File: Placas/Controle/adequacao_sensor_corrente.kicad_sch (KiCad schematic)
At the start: 10 parts, among them J8 Conn_01x03_Pin, U6 LM324

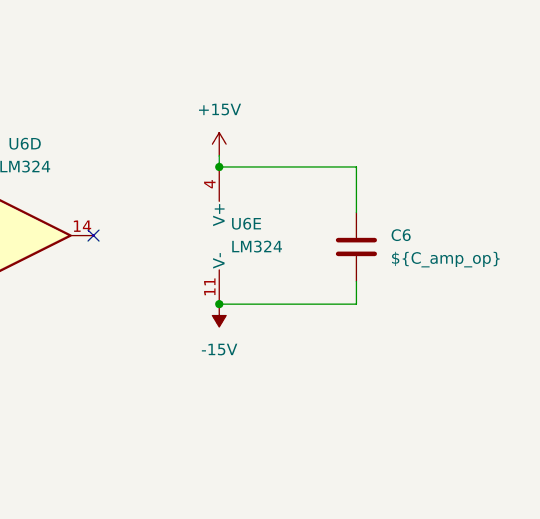
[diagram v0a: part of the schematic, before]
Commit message: Adição de circuitos opcionais para PWM
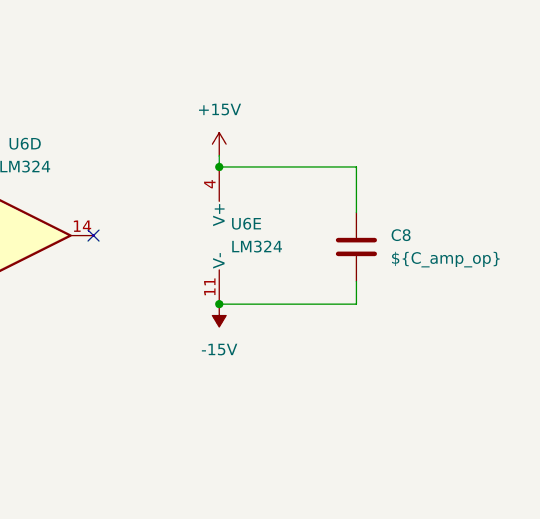
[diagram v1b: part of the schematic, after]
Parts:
- renumbered C6 to C8
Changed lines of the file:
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@@
 		(dnp no)
 		(fields_autoplaced yes)
-		(property "Reference" "#PWR38"
+		(property "Reference" "#PWR40"
 			(at 53.34 63.5 0)
 			(effects
@@
 			(project "board"
 				(path "/01568b53-f202-4f02-9c1a-9c10c7610b4b/64ed1ee1-6201-4cd1-840c-b46b599d55ab/0ec4e805-f770-43f6-9ceb-79230d0ce8bc"
-					(reference "#PWR38")
+					(reference "#PWR40")
 					(unit 1)
 				)
 				(path "/01568b53-f202-4f02-9c1a-9c10c7610b4b/64ed1ee1-6201-4cd1-840c-b46b599d55ab/23b832df-fa68-4730-aab0-9fb63a0aaa4a"
-					(reference "#PWR46")
+					(reference "#PWR48")
 					(unit 1)
 				)
 				(path "/01568b53-f202-4f02-9c1a-9c10c7610b4b/64ed1ee1-6201-4cd1-840c-b46b599d55ab/54eee298-1ebc-4f78-aeba-50023d2029d6"
-					(reference "#PWR22")
+					(reference "#PWR24")
 					(unit 1)
 				)
 				(path "/01568b53-f202-4f02-9c1a-9c10c7610b4b/64ed1ee1-6201-4cd1-840c-b46b599d55ab/6bc42b43-1f09-4868-86cc-13b6bc39566b"
-					(reference "#PWR30")
+					(reference "#PWR32")
 					(unit 1)
 				)
@@
 		(dnp no)
 		(fields_autoplaced yes)
-		(property "Reference" "#PWR43"
+		(property "Reference" "#PWR45"
 			(at 207.01 85.09 0)
 			(effects
@@
 			(project "board"
 				(path "/01568b53-f202-4f02-9c1a-9c10c7610b4b/64ed1ee1-6201-4cd1-840c-b46b599d55ab/0ec4e805-f770-43f6-9ceb-79230d0ce8bc"
-					(reference "#PWR43")
+					(reference "#PWR45")
 					(unit 1)
 				)
 				(path "/01568b53-f202-4f02-9c1a-9c10c7610b4b/64ed1ee1-6201-4cd1-840c-b46b599d55ab/23b832df-fa68-4730-aab0-9fb63a0aaa4a"
-					(reference "#PWR51")
+					(reference "#PWR53")
 					(unit 1)
 				)
 				(path "/01568b53-f202-4f02-9c1a-9c10c7610b4b/64ed1ee1-6201-4cd1-840c-b46b599d55ab/54eee298-1ebc-4f78-aeba-50023d2029d6"
-					(reference "#PWR27")
+					(reference "#PWR29")
 					(unit 1)
 				)
 				(path "/01568b53-f202-4f02-9c1a-9c10c7610b4b/64ed1ee1-6201-4cd1-840c-b46b599d55ab/6bc42b43-1f09-4868-86cc-13b6bc39566b"
-					(reference "#PWR35")
+					(reference "#PWR37")
 					(unit 1)
 				)
@@
 		(dnp no)
 		(fields_autoplaced yes)
-		(property "Reference" "C6"
+		(property "Reference" "C8"
 			(at 226.06 81.2799 0)
 			(effects
@@
 			(project "board"
 				(path "/01568b53-f202-4f02-9c1a-9c10c7610b4b/64ed1ee1-6201-4cd1-840c-b46b599d55ab/0ec4e805-f770-43f6-9ceb-79230d0ce8bc"
+					(reference "C8")
+					(unit 1)
+				)
+				(path "/01568b53-f202-4f02-9c1a-9c10c7610b4b/64ed1ee1-6201-4cd1-840c-b46b599d55ab/23b832df-fa68-4730-aab0-9fb63a0aaa4a"
+					(reference "C9")
+					(unit 1)
+				)
+				(path "/01568b53-f202-4f02-9c1a-9c10c7610b4b/64ed1ee1-6201-4cd1-840c-b46b599d55ab/54eee298-1ebc-4f78-aeba-50023d2029d6"
 					(reference "C6")
 					(unit 1)
 				)
-				(path "/01568b53-f202-4f02-9c1a-9c10c7610b4b/64ed1ee1-6201-4cd1-840c-b46b599d55ab/23b832df-fa68-4730-aab0-9fb63a0aaa4a"
+				(path "/01568b53-f202-4f02-9c1a-9c10c7610b4b/64ed1ee1-6201-4cd1-840c-b46b599d55ab/6bc42b43-1f09-4868-86cc-13b6bc39566b"
 					(reference "C7")
-					(unit 1)
-				)
-				(path "/01568b53-f202-4f02-9c1a-9c10c7610b4b/64ed1ee1-6201-4cd1-840c-b46b599d55ab/54eee298-1ebc-4f78-aeba-50023d2029d6"
-					(reference "C4")
-					(unit 1)
-				)
-				(path "/01568b53-f202-4f02-9c1a-9c10c7610b4b/64ed1ee1-6201-4cd1-840c-b46b599d55ab/6bc42b43-1f09-4868-86cc-13b6bc39566b"
-					(reference "C5")
 					(unit 1)
 				)
@@
 		(dnp no)
 		(fields_autoplaced yes)
-		(property "Reference" "#PWR36"
+		(property "Reference" "#PWR38"
 			(at 52.07 83.82 0)
 			(effects
@@
 			(project "board"
 				(path "/01568b53-f202-4f02-9c1a-9c10c7610b4b/64ed1ee1-6201-4cd1-840c-b46b599d55ab/0ec4e805-f770-43f6-9ceb-79230d0ce8bc"
-					(reference "#PWR36")
+					(reference "#PWR38")
 					(unit 1)
 				)
 				(path "/01568b53-f202-4f02-9c1a-9c10c7610b4b/64ed1ee1-6201-4cd1-840c-b46b599d55ab/23b832df-fa68-4730-aab0-9fb63a0aaa4a"
-					(reference "#PWR44")
+					(reference "#PWR46")
 					(unit 1)
 				)
 				(path "/01568b53-f202-4f02-9c1a-9c10c7610b4b/64ed1ee1-6201-4cd1-840c-b46b599d55ab/54eee298-1ebc-4f78-aeba-50023d2029d6"
-					(reference "#PWR20")
+					(reference "#PWR22")
 					(unit 1)
 				)
 				(path "/01568b53-f202-4f02-9c1a-9c10c7610b4b/64ed1ee1-6201-4cd1-840c-b46b599d55ab/6bc42b43-1f09-4868-86cc-13b6bc39566b"
-					(reference "#PWR28")
+					(reference "#PWR30")
 					(unit 1)
 				)
@@
 		(dnp no)
 		(fields_autoplaced yes)
-		(property "Reference" "#PWR41"
+		(property "Reference" "#PWR43"
 			(at 121.92 104.14 0)
 			(effects
@@
 			(project "board"
 				(path "/01568b53-f202-4f02-9c1a-9c10c7610b4b/64ed1ee1-6201-4cd1-840c-b46b599d55ab/0ec4e805-f770-43f6-9ceb-79230d0ce8bc"
-					(reference "#PWR41")
+					(reference "#PWR43")
 					(unit 1)
 				)
 				(path "/01568b53-f202-4f02-9c1a-9c10c7610b4b/64ed1ee1-6201-4cd1-840c-b46b599d55ab/23b832df-fa68-4730-aab0-9fb63a0aaa4a"
-					(reference "#PWR49")
+					(reference "#PWR51")
 					(unit 1)
 				)
 				(path "/01568b53-f202-4f02-9c1a-9c10c7610b4b/64ed1ee1-6201-4cd1-840c-b46b599d55ab/54eee298-1ebc-4f78-aeba-50023d2029d6"
-					(reference "#PWR25")
+					(reference "#PWR27")
 					(unit 1)
 				)
 				(path "/01568b53-f202-4f02-9c1a-9c10c7610b4b/64ed1ee1-6201-4cd1-840c-b46b599d55ab/6bc42b43-1f09-4868-86cc-13b6bc39566b"
-					(reference "#PWR33")
+					(reference "#PWR35")
 					(unit 1)
 				)
@@
 		(dnp no)
 		(fields_autoplaced yes)
-		(property "Reference" "#PWR40"
+		(property "Reference" "#PWR42"
 			(at 67.31 85.09 0)
 			(effects
@@
 			(project "board"
 				(path "/01568b53-f202-4f02-9c1a-9c10c7610b4b/64ed1ee1-6201-4cd1-840c-b46b599d55ab/0ec4e805-f770-43f6-9ceb-79230d0ce8bc"
-					(reference "#PWR40")
+					(reference "#PWR42")
 					(unit 1)
 				)
 				(path "/01568b53-f202-4f02-9c1a-9c10c7610b4b/64ed1ee1-6201-4cd1-840c-b46b599d55ab/23b832df-fa68-4730-aab0-9fb63a0aaa4a"
-					(reference "#PWR48")
+					(reference "#PWR50")
 					(unit 1)
 				)
 				(path "/01568b53-f202-4f02-9c1a-9c10c7610b4b/64ed1ee1-6201-4cd1-840c-b46b599d55ab/54eee298-1ebc-4f78-aeba-50023d2029d6"
-					(reference "#PWR24")
+					(reference "#PWR26")
 					(unit 1)
 				)
 				(path "/01568b53-f202-4f02-9c1a-9c10c7610b4b/64ed1ee1-6201-4cd1-840c-b46b599d55ab/6bc42b43-1f09-4868-86cc-13b6bc39566b"
-					(reference "#PWR32")
+					(reference "#PWR34")
 					(unit 1)
 				)
@@
 		(dnp no)
 		(fields_autoplaced yes)
-		(property "Reference" "#PWR39"
+		(property "Reference" "#PWR41"
 			(at 53.34 68.58 0)
 			(effects
@@
 			(project "board"
 				(path "/01568b53-f202-4f02-9c1a-9c10c7610b4b/64ed1ee1-6201-4cd1-840c-b46b599d55ab/0ec4e805-f770-43f6-9ceb-79230d0ce8bc"
-					(reference "#PWR39")
+					(reference "#PWR41")
 					(unit 1)
 				)
 				(path "/01568b53-f202-4f02-9c1a-9c10c7610b4b/64ed1ee1-6201-4cd1-840c-b46b599d55ab/23b832df-fa68-4730-aab0-9fb63a0aaa4a"
-					(reference "#PWR47")
+					(reference "#PWR49")
 					(unit 1)
 				)
 				(path "/01568b53-f202-4f02-9c1a-9c10c7610b4b/64ed1ee1-6201-4cd1-840c-b46b599d55ab/54eee298-1ebc-4f78-aeba-50023d2029d6"
-					(reference "#PWR23")
+					(reference "#PWR25")
 					(unit 1)
 				)
 				(path "/01568b53-f202-4f02-9c1a-9c10c7610b4b/64ed1ee1-6201-4cd1-840c-b46b599d55ab/6bc42b43-1f09-4868-86cc-13b6bc39566b"
-					(reference "#PWR31")
+					(reference "#PWR33")
 					(unit 1)
 				)
@@
 		(dnp no)
 		(fields_autoplaced yes)
-		(property "Reference" "#PWR37"
+		(property "Reference" "#PWR39"
 			(at 52.07 115.57 0)
 			(effects
@@
 			(project "board"
 				(path "/01568b53-f202-4f02-9c1a-9c10c7610b4b/64ed1ee1-6201-4cd1-840c-b46b599d55ab/0ec4e805-f770-43f6-9ceb-79230d0ce8bc"
-					(reference "#PWR37")
+					(reference "#PWR39")
 					(unit 1)
 				)
 				(path "/01568b53-f202-4f02-9c1a-9c10c7610b4b/64ed1ee1-6201-4cd1-840c-b46b599d55ab/23b832df-fa68-4730-aab0-9fb63a0aaa4a"
-					(reference "#PWR45")
+					(reference "#PWR47")
 					(unit 1)
 				)
 				(path "/01568b53-f202-4f02-9c1a-9c10c7610b4b/64ed1ee1-6201-4cd1-840c-b46b599d55ab/54eee298-1ebc-4f78-aeba-50023d2029d6"
-					(reference "#PWR21")
+					(reference "#PWR23")
 					(unit 1)
 				)
 				(path "/01568b53-f202-4f02-9c1a-9c10c7610b4b/64ed1ee1-6201-4cd1-840c-b46b599d55ab/6bc42b43-1f09-4868-86cc-13b6bc39566b"
-					(reference "#PWR29")
+					(reference "#PWR31")
 					(unit 1)
 				)
@@
 		(dnp no)
 		(fields_autoplaced yes)
-		(property "Reference" "#PWR42"
+		(property "Reference" "#PWR44"
 			(at 207.01 76.2 0)
 			(effects
@@
 			(project "board"
 				(path "/01568b53-f202-4f02-9c1a-9c10c7610b4b/64ed1ee1-6201-4cd1-840c-b46b599d55ab/0ec4e805-f770-43f6-9ceb-79230d0ce8bc"
-					(reference "#PWR42")
+					(reference "#PWR44")
 					(unit 1)
 				)
 				(path "/01568b53-f202-4f02-9c1a-9c10c7610b4b/64ed1ee1-6201-4cd1-840c-b46b599d55ab/23b832df-fa68-4730-aab0-9fb63a0aaa4a"
-					(reference "#PWR50")
+					(reference "#PWR52")
 					(unit 1)
 				)
 				(path "/01568b53-f202-4f02-9c1a-9c10c7610b4b/64ed1ee1-6201-4cd1-840c-b46b599d55ab/54eee298-1ebc-4f78-aeba-50023d2029d6"
-					(reference "#PWR26")
+					(reference "#PWR28")
 					(unit 1)
 				)
 				(path "/01568b53-f202-4f02-9c1a-9c10c7610b4b/64ed1ee1-6201-4cd1-840c-b46b599d55ab/6bc42b43-1f09-4868-86cc-13b6bc39566b"
-					(reference "#PWR34")
-					(unit 1)
-				)
+					(reference "#PWR36")
+					(unit 1)
+				)

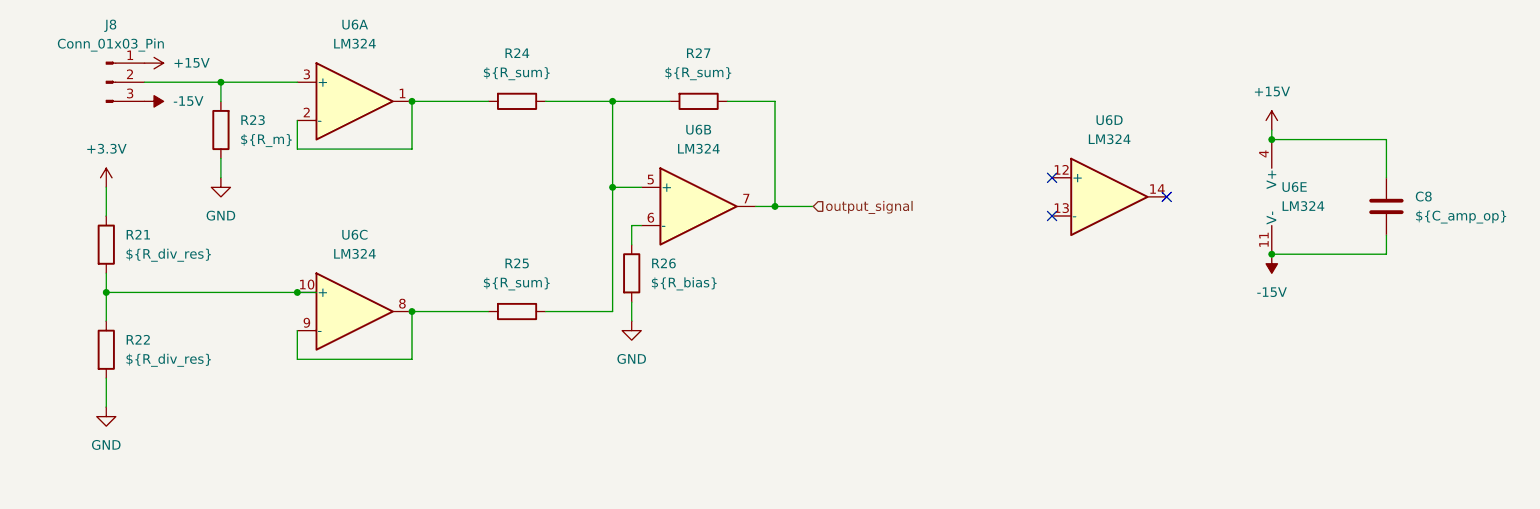
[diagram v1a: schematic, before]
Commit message: Modificações nas duas placas, adição de furos para montagem, melhora na posição dos micros e conectores para comunicação SPI
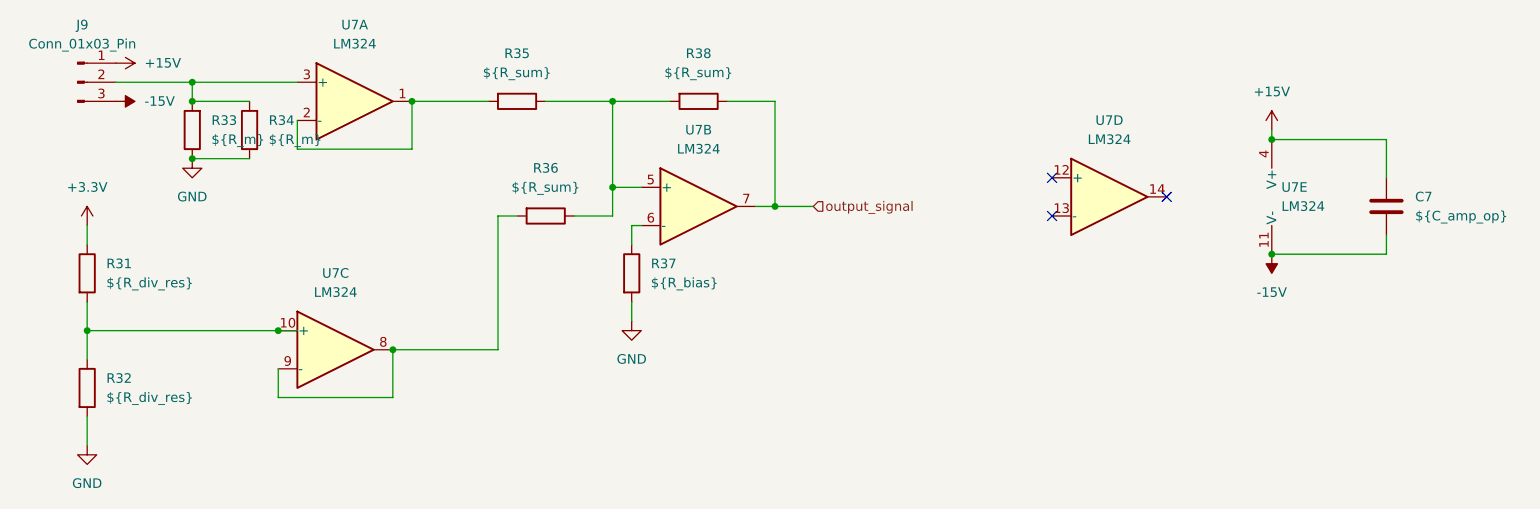
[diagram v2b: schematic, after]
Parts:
- added R34: ${R_m}, Resistor_SMD:R_0805_2012Metric_Pad1.20x1.40mm_HandSolder, symbol Device:R
- C7: renamed from C8; footprint Capacitor_THT:C_Disc_D8.0mm_W5.0mm_P7.50mm -> Capacitor_SMD:C_0805_2012Metric_Pad1.18x1.45mm_HandSolder
- R31: renamed from R21; footprint Resistor_THT:R_Axial_DIN0207_L6.3mm_D2.5mm_P7.62mm_Horizontal -> Resistor_SMD:R_0805_2012Metric_Pad1.20x1.40mm_HandSolder
- R32: renamed from R22; footprint Resistor_THT:R_Axial_DIN0207_L6.3mm_D2.5mm_P7.62mm_Horizontal -> Resistor_SMD:R_0805_2012Metric_Pad1.20x1.40mm_HandSolder
- R33: renamed from R23; footprint Resistor_THT:R_Axial_DIN0207_L6.3mm_D2.5mm_P7.62mm_Horizontal -> Resistor_SMD:R_0805_2012Metric_Pad1.20x1.40mm_HandSolder
- R35: renamed from R24; footprint Resistor_THT:R_Axial_DIN0207_L6.3mm_D2.5mm_P7.62mm_Horizontal -> Resistor_SMD:R_0805_2012Metric_Pad1.20x1.40mm_HandSolder
- R36: renamed from R25; footprint Resistor_THT:R_Axial_DIN0207_L6.3mm_D2.5mm_P7.62mm_Horizontal -> Resistor_SMD:R_0805_2012Metric_Pad1.20x1.40mm_HandSolder
- R37: renamed from R26; footprint Resistor_THT:R_Axial_DIN0207_L6.3mm_D2.5mm_P7.62mm_Horizontal -> Resistor_SMD:R_0805_2012Metric_Pad1.20x1.40mm_HandSolder
- R38: renamed from R27; footprint Resistor_THT:R_Axial_DIN0207_L6.3mm_D2.5mm_P7.62mm_Horizontal -> Resistor_SMD:R_0805_2012Metric_Pad1.20x1.40mm_HandSolder
- renumbered J8 to J9, U6 to U7
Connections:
- net GND: now also R34.1
- net at J9.2 (Pin_2), R33.2, U7.3 (+): now also R34.2
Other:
- moved on the sheet: J9, R31, R32, R33, R36, U7C

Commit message: Mudanças no firmware e calibração da tensão de entrada e saída
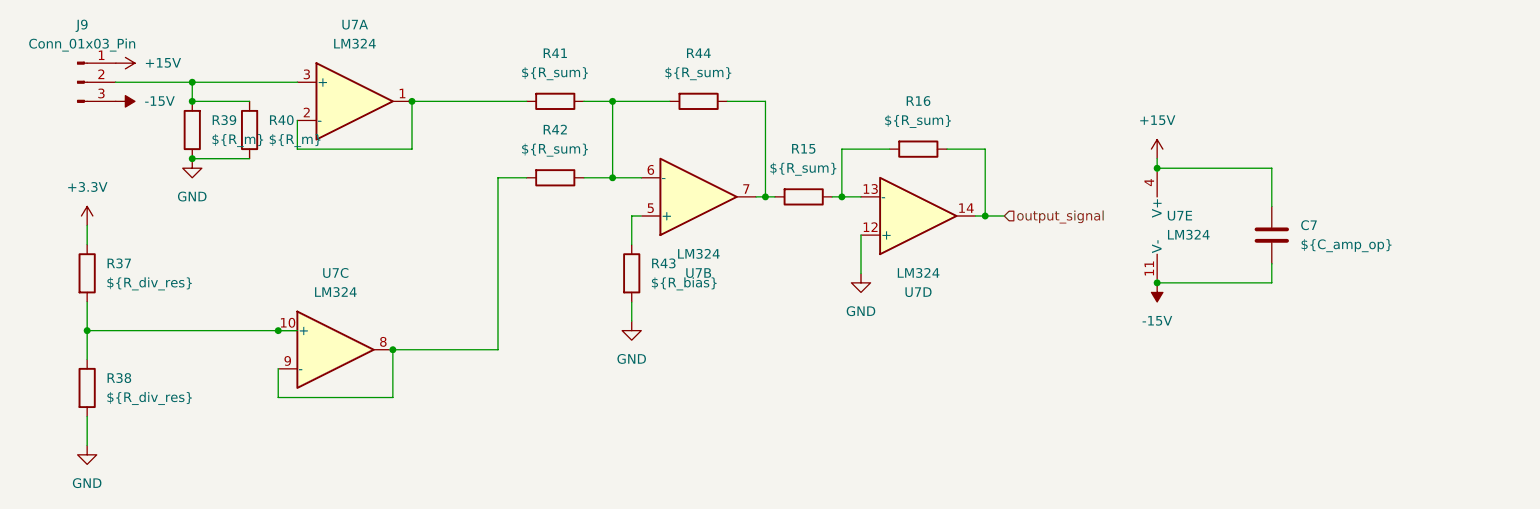
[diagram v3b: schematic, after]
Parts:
- added R15, R16: ${R_sum}, Resistor_SMD:R_0805_2012Metric_Pad1.20x1.40mm_HandSolder, symbol Device:R
- renumbered R31 to R37, R32 to R38, R33 to R39, R34 to R40, R35 to R41, R36 to R42, R37 to R43, R38 to R44
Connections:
- net GND: now also U7.12 (+)
- net output_signal: now also U7.14, R16.1; no longer R44.1, U7.7
- net at R41.1, R42.1, R44.2: now also U7.6 (-); no longer U7.5 (+)
- net at R43.1: now also U7.5 (+); no longer U7.6 (-)
- net at U7.13 (-): now also R15.1, R16.2
- new net: R15.2, R44.1, U7.7
- no-connect marks 3 -> 0
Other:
- moved on the sheet: C7, R41, R42, U7B, U7D, U7E
